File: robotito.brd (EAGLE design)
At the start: 80 x 84 mm, 46 parts, among them IC1 7805T, IC2 L298POWERSO-20, IC3 L298POWERSO-20

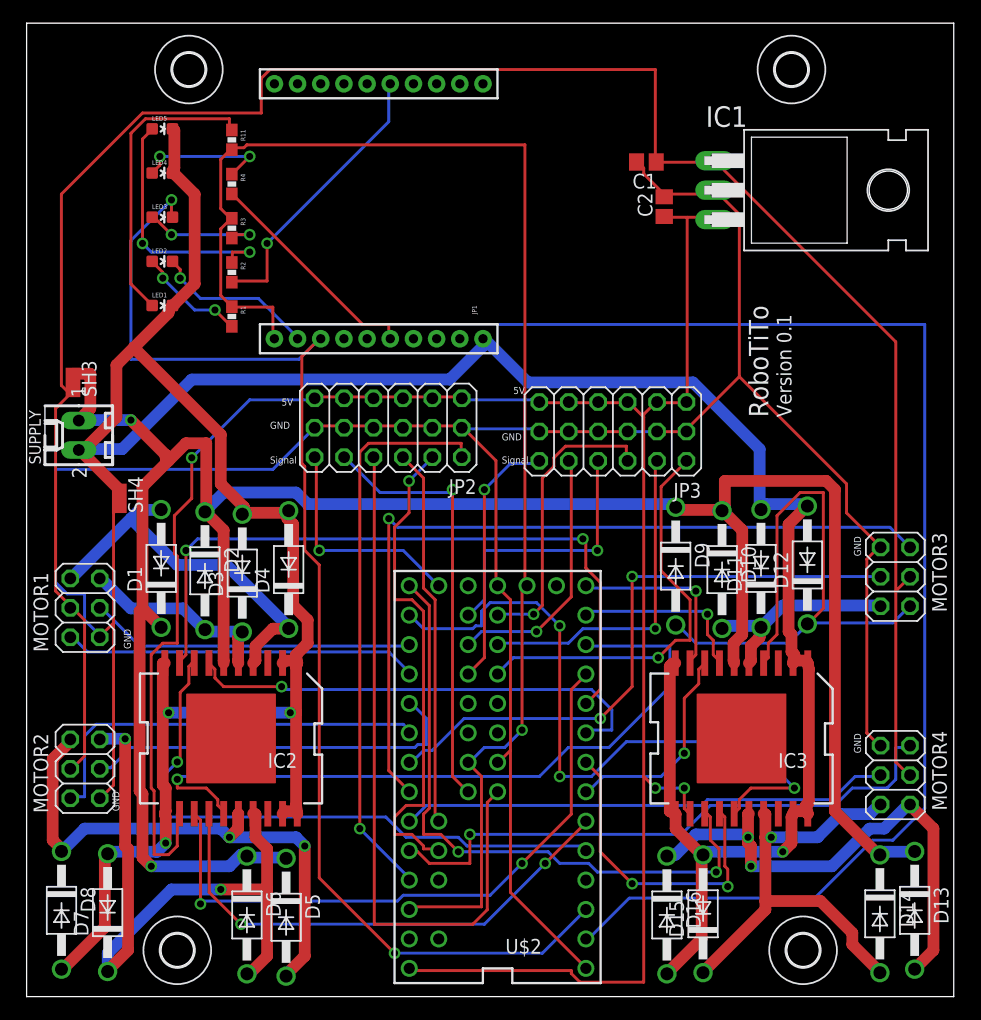
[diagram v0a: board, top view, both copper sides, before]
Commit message: Fix separation to comply with pcbway. V1 sent to print
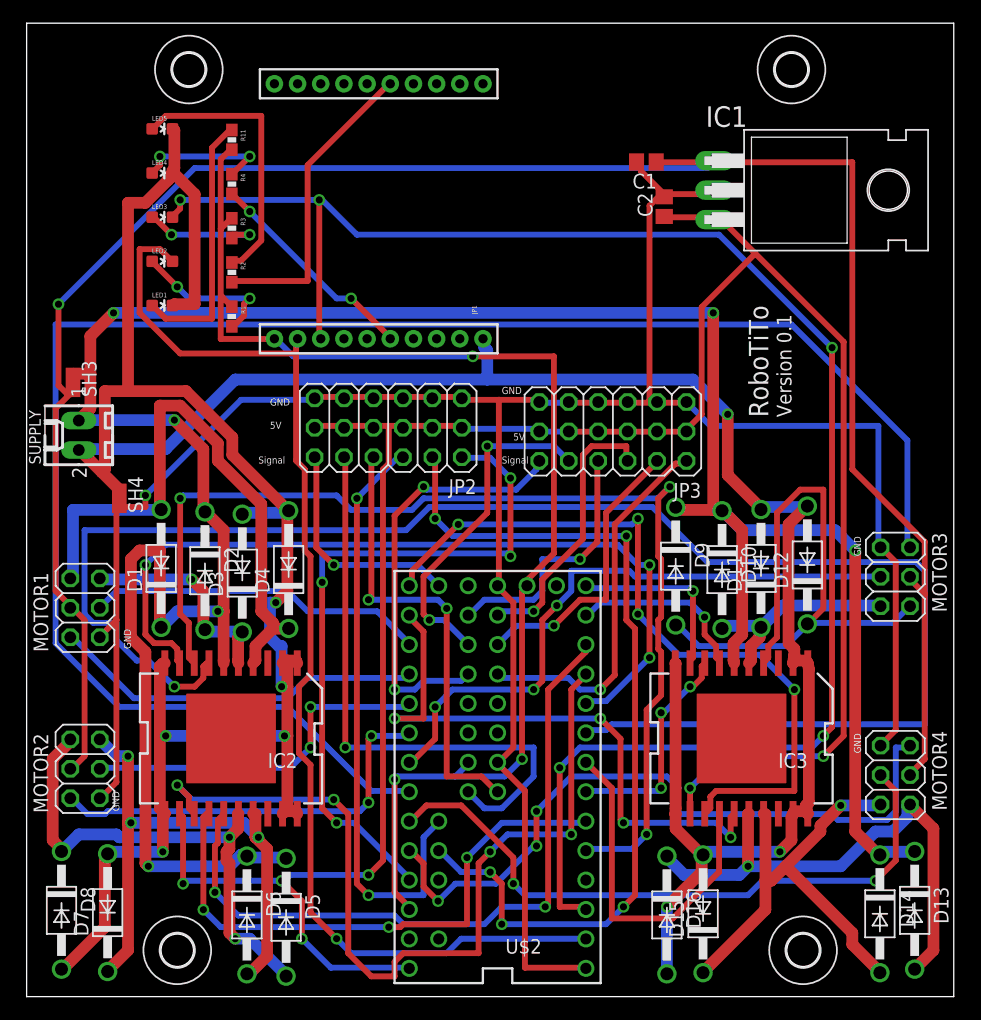
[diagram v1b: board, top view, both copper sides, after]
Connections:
- net +5V: now also JP2.P11, JP2.P14, JP2.P17, JP2.P2, JP2.P5, JP2.P8, JP3.P11, JP3.P14, JP3.P17, JP3.P2, JP3.P5, JP3.P8; no longer JP2.P12, JP2.P15, JP2.P18, JP2.P3, JP2.P6, JP2.P9, JP3.P12, JP3.P15, JP3.P18, JP3.P3, JP3.P6, JP3.P9
- net LPGND: now also JP2.P12, JP2.P15, JP2.P18, JP2.P3, JP2.P6, JP2.P9, JP3.P12, JP3.P15, JP3.P18, JP3.P3, JP3.P6, JP3.P9; no longer JP2.P11, JP2.P14, JP2.P17, JP2.P2, JP2.P5, JP2.P8, JP3.P11, JP3.P14, JP3.P17, JP3.P2, JP3.P5, JP3.P8
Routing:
- net M1I1: track 41.0 -> 141.3 mm
- net M3ENCB: track 70.3 -> 150.3 mm, vias 1 -> 0
- net RX: track 145.0 -> 100.4 mm
- net M1EN: track 51.9 -> 95.5 mm, vias 1 -> 3
- net TX: track 109.0 -> 147.5 mm, vias 2 -> 5
- net DS2: track 42.3 -> 76.6 mm, vias 1 -> 5
- net VCC: track 198.8 -> 228.3 mm, vias 2 -> 6
- net DS4: track 61.1 -> 39.0 mm, vias 0 -> 2
- net M2I1: track 55.8 -> 75.6 mm, vias 2 -> 4
- net M1M1: track 32.9 -> 52.0 mm
- net DS3: track 32.7 -> 51.8 mm, vias 0 -> 2
- net GND: track 283.2 -> 301.6 mm, vias 4 -> 8
- net +5V: track 185.3 -> 200.2 mm, vias 3 -> 6
- net DS12: track 22.3 -> 36.8 mm, vias 1 -> 2
- net M4ENCA: track 42.3 -> 56.2 mm, vias 0 -> 2
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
